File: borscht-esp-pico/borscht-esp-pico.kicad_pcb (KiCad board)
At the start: 2 copper layers, 57.2 x 22.6 mm, 29 parts, among them J1 USB, J2 GPIO, J3 GPIO, J4 VUSB, Q1 S8050, Q2 S8050, SW1 BOOT, SW2 RESET, U1 ESP32-PICO-D4, U2 ESP-PSRAM32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

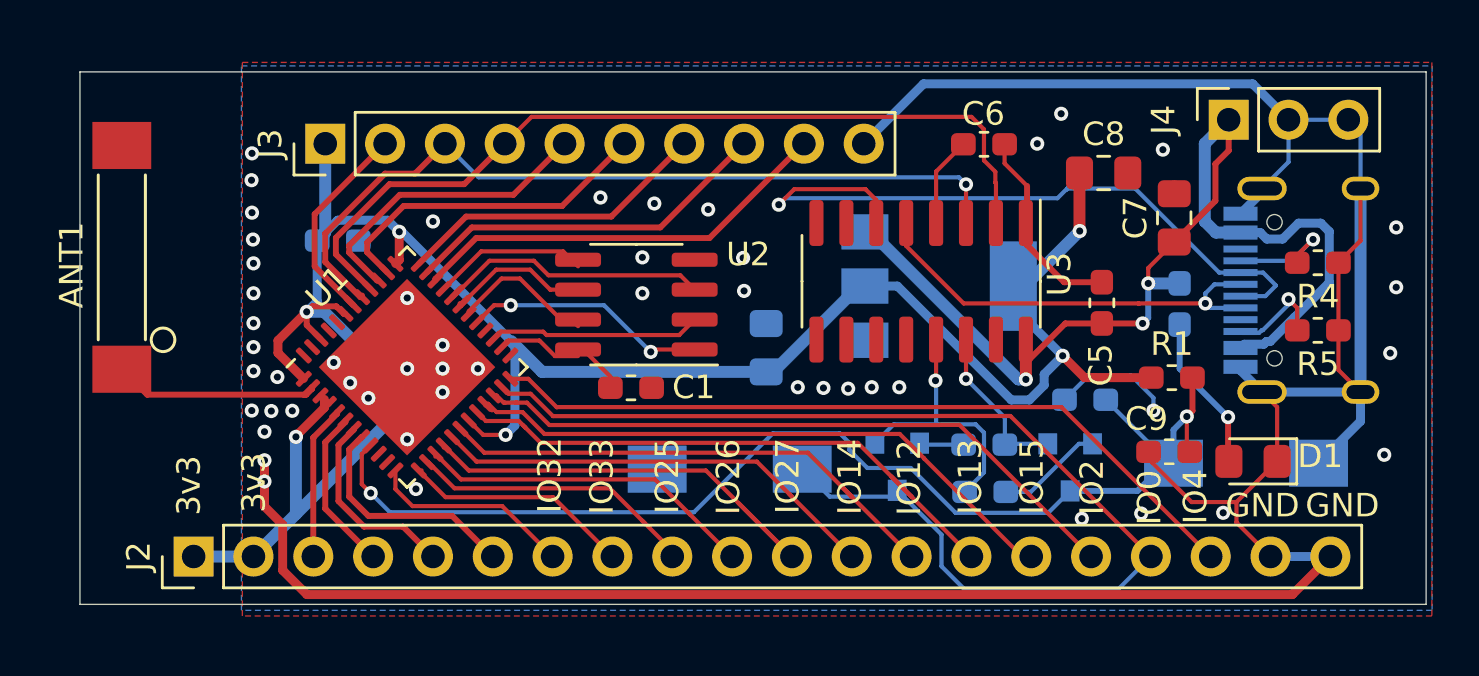
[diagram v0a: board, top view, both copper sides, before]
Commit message: Add 99x99mm, 4x1 panel
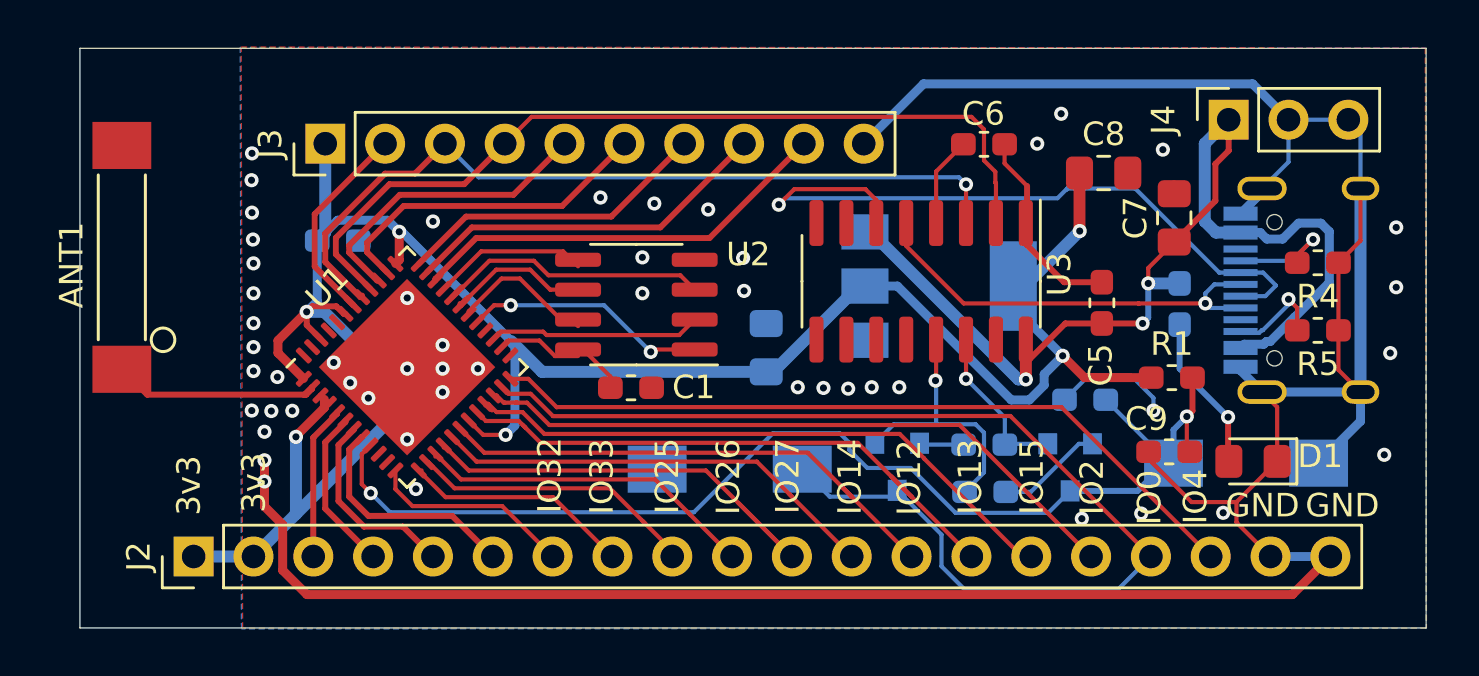
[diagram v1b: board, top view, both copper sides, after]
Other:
- board size 57.2 x 22.6 mm -> 57.2 x 24.6 mm
